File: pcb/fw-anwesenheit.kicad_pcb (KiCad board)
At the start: 6 copper layers, 50 x 50 mm, 48 parts, among them J1 Conn_01x02_Pin, J2 I2C, J3 LED, J4 MicroSD, U1 XIAO-ESP32-S3-SMD, U2 SN74AHCT1G125DBVT, U3 DS3231M

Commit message: changed via size
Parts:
- TP6: value SD_DECT -> DECT
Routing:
- net Net-(U1-GPIO16_D6_TX): track 41.7 -> 42.3 mm
- net GND: vias 107 -> 108

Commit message: changed some pcb descriptions and Resistor for LED
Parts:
- C2, C3: value 100 nF -> 100nF
- R1: value 100R -> 150R
- TP6: value DECT -> SD_DECT

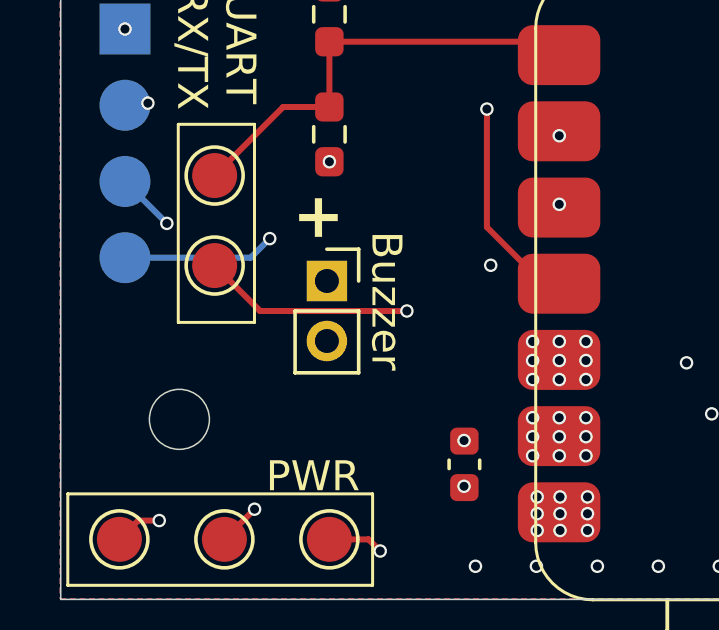
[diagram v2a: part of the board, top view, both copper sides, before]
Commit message: fixed buzzer footprint
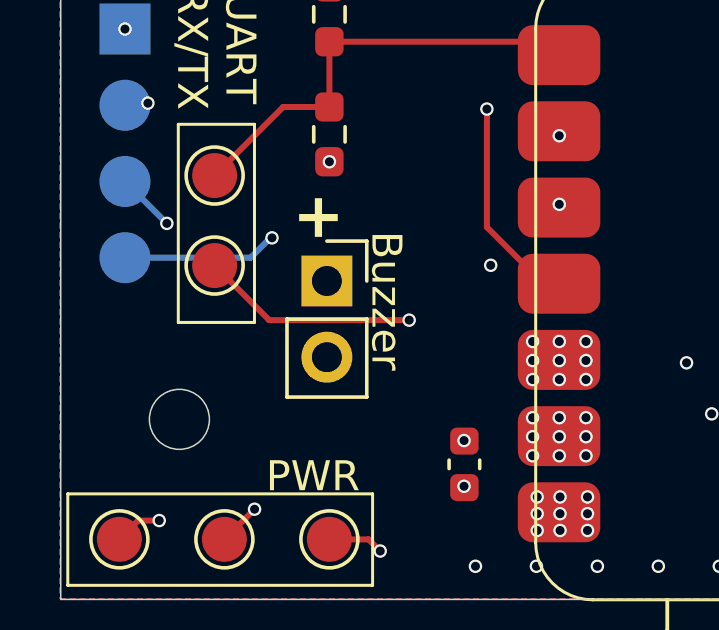
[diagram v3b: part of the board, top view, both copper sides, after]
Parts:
- BZ1: footprint Connector_PinSocket_2.00mm:PinSocket_1x02_P2.00mm_Vertical -> Connector_PinSocket_2.54mm:PinSocket_1x02_P2.54mm_Vertical
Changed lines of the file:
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@@
 		)
 	)
-	(footprint "Connector_PinSocket_2.00mm:PinSocket_1x02_P2.00mm_Vertical"
+	(footprint "Connector_PinSocket_2.54mm:PinSocket_1x02_P2.54mm_Vertical"
 		(layer "F.Cu")
 		(at 89.916 118.888)
-		(descr "Through hole straight socket strip, 1x02, 2.00mm pitch, single row (from Kicad 4.0.7), script generated")
-		(tags "Through hole socket strip THT 1x02 2.00mm single row")
+		(descr "Through hole straight socket strip, 1x02, 2.54mm pitch, single row (from Kicad 4.0.7), script generated")
+		(tags "Through hole socket strip THT 1x02 2.54mm single row")
 		(property "Reference" "BZ1"
-			(at 0 -2.5 0)
+			(at 0 -2.77 0)
 			(layer "F.SilkS")
 			(hide yes)
@@
 		)
 		(property "Value" "Buzzer"
-			(at 0 4.5 0)
+			(at 0 5.31 0)
 			(layer "F.Fab")
 			(hide yes)
@@
 		(attr through_hole)
 		(fp_line
-			(start -1.06 1)
-			(end -1.06 3.06)
+			(start -1.33 1.27)
+			(end -1.33 3.87)
 			(stroke
 				(width 0.12)
@@
 		)
 		(fp_line
-			(start -1.06 1)
-			(end 1.06 1)
+			(start -1.33 1.27)
+			(end 1.33 1.27)
 			(stroke
 				(width 0.12)
@@
 		)
 		(fp_line
-			(start -1.06 3.06)
-			(end 1.06 3.06)
+			(start -1.33 3.87)
+			(end 1.33 3.87)
 			(stroke
 				(width 0.12)
@@
 		)
 		(fp_line
-			(start 0 -1.06)
-			(end 1.06 -1.06)
+			(start 0 -1.33)
+			(end 1.33 -1.33)
 			(stroke
 				(width 0.12)
@@
 		)
 		(fp_line
-			(start 1.06 -1.06)
-			(end 1.06 0)
+			(start 1.33 -1.33)
+			(end 1.33 0)
 			(stroke
 				(width 0.12)
@@
 		)
 		(fp_line
-			(start 1.06 1)
-			(end 1.06 3.06)
+			(start 1.33 1.27)
+			(end 1.33 3.87)
 			(stroke
 				(width 0.12)
@@
 		)
 		(fp_line
-			(start -1.5 -1.5)
-			(end 1.5 -1.5)
+			(start -1.8 -1.8)
+			(end 1.75 -1.8)
 			(stroke
 				(width 0.05)
@@
 		)
 		(fp_line
-			(start -1.5 3.5)
-			(end -1.5 -1.5)
+			(start -1.8 4.3)
+			(end -1.8 -1.8)
 			(stroke
 				(width 0.05)
@@
 		)
 		(fp_line
-			(start 1.5 -1.5)
-			(end 1.5 3.5)
+			(start 1.75 -1.8)
+			(end 1.75 4.3)
 			(stroke
 				(width 0.05)
@@
 		)
 		(fp_line
-			(start 1.5 3.5)
-			(end -1.5 3.5)
+			(start 1.75 4.3)
+			(end -1.8 4.3)
 			(stroke
 				(width 0.05)
@@
 		)
 		(fp_line
-			(start -1 -1)
-			(end 0.5 -1)
+			(start -1.27 -1.27)
+			(end 0.635 -1.27)
 			(stroke
 				(width 0.1)
@@
 		)
 		(fp_line
-			(start -1 3)
-			(end -1 -1)
+			(start -1.27 3.81)
+			(end -1.27 -1.27)
 			(stroke
 				(width 0.1)
@@
 		)
 		(fp_line
-			(start 0.5 -1)
-			(end 1 -0.5)
+			(start 0.635 -1.27)
+			(end 1.27 -0.635)
 			(stroke
 				(width 0.1)
@@
 		)
 		(fp_line
-			(start 1 -0.5)
-			(end 1 3)
+			(start 1.27 -0.635)
+			(end 1.27 3.81)
 			(stroke
 				(width 0.1)
@@
 		)
 		(fp_line
-			(start 1 3)
-			(end -1 3)
+			(start 1.27 3.81)
+			(end -1.27 3.81)
 			(stroke
 				(width 0.1)
@@
 		)
 		(fp_text user "${REFERENCE}"
-			(at 0 1 90)
+			(at 0 1.27 90)
 			(layer "F.Fab")
 			(effects
@@
 		(pad "1" thru_hole rect
 			(at 0 0)
-			(size 1.35 1.35)
-			(drill 0.8)
+			(size 1.7 1.7)
+			(drill 1)
 			(layers "*.Cu" "*.Mask")
-			(remove_unused_layers yes)
-			(keep_end_layers yes)
-			(zone_layer_connections)
+			(remove_unused_layers no)
 			(net 18 "/Buzzer")
 			(pinfunction "+")
@@
 		)
 		(pad "2" thru_hole circle
-			(at 0 2)
-			(size 1.35 1.35)
-			(drill 0.8)
+			(at 0 2.54)
+			(size 1.7 1.7)
+			(drill 1)
 			(layers "*.Cu" "*.Mask")
-			(remove_unused_layers yes)
-			(keep_end_layers yes)
-			(zone_layer_connections "In1.Cu" "In2.Cu" "In3.Cu" "In4.Cu")
+			(remove_unused_layers no)
 			(net 1 "GND")
 			(pinfunction "-")
@@
 		)
 		(embedded_fonts no)
-		(model "${KICAD9_3DMODEL_DIR}/Connector_PinSocket_2.00mm.3dshapes/PinSocket_1x02_P2.00mm_Vertical.step"
+		(model "${KICAD9_3DMODEL_DIR}/Connector_PinSocket_2.54mm.3dshapes/PinSocket_1x02_P2.54mm_Vertical.step"
 			(offset
 				(xyz 0 0 0)
@@
 	)
 	(segment
-		(start 116.459 118.11)
-		(end 116.459 113.9959)
+		(start 87.9948 120.1928)
+		(end 86.302 118.5)
 		(width 0.2)
 		(layer "F.Cu")
@@
 	)
 	(segment
-		(start 116.459 113.9959)
-		(end 113.8216 111.3585)
+		(start 116.459 118.11)
+		(end 116.459 113.9959)
 		(width 0.2)
 		(layer "F.Cu")
@@
 	)
 	(segment
-		(start 116.078 118.491)
-		(end 116.459 118.11)
+		(start 92.6592 120.1928)
+		(end 87.9948 120.1928)
 		(width 0.2)
 		(layer "F.Cu")
@@
 	)
 	(segment
-		(start 87.69 119.888)
-		(end 92.583 119.888)
+		(start 116.459 113.9959)
+		(end 113.8216 111.3585)
 		(width 0.2)
 		(layer "F.Cu")
@@
 	)
 	(segment
-		(start 86.302 118.5)
-		(end 87.69 119.888)
+		(start 116.078 118.491)
+		(end 116.459 118.11)
 		(width 0.2)
 		(layer "F.Cu")
@@
 	)
 	(via
-		(at 92.583 119.888)
+		(at 92.6592 120.1928)
 		(size 0.45)
 		(drill 0.3)
@@
 	)
 	(segment
-		(start 103.4796 122.0216)
-		(end 101.346 119.888)
+		(start 114.5794 122.0216)
+		(end 116.078 120.523)
 		(width 0.2)
 		(layer "In3.Cu")
@@
 	)
 	(segment
-		(start 114.5794 122.0216)
-		(end 103.4796 122.0216)
+		(start 103.4796 122.0216)
+		(end 114.5794 122.0216)
 		(width 0.2)
 		(layer "In3.Cu")
@@
 	)
 	(segment
-		(start 116.078 120.523)
-		(end 114.5794 122.0216)
+		(start 92.6592 120.1928)
+		(end 101.6508 120.1928)
 		(width 0.2)
 		(layer "In3.Cu")
@@
 	)
 	(segment
-		(start 116.078 118.491)
-		(end 116.078 120.523)
+		(start 101.6508 120.1928)
+		(end 103.4796 122.0216)
 		(width 0.2)
 		(layer "In3.Cu")
@@
 	)
 	(segment
-		(start 101.346 119.888)
-		(end 92.583 119.888)
+		(start 116.078 120.523)
+		(end 116.078 118.491)
 		(width 0.2)
 		(layer "In3.Cu")
@@
 	)
 	(via
-		(at 88.011 117.475)
+		(at 88.0872 117.4496)
 		(size 0.45)
 		(drill 0.3)
@@
 	)
 	(segment
-		(start 83.185 118.11)
-		(end 87.376 118.11)
+		(start 87.376 118.11)
+		(end 83.185 118.11)
 		(width 0.2)
 		(layer "B.Cu")
@@
 	)
 	(segment
-		(start 87.376 118.11)
-		(end 88.011 117.475)
+		(start 88.0872 117.4496)
+		(end 88.0364 117.4496)
 		(width 0.2)
 		(layer "B.Cu")
@@
 	)
 	(segment
-		(start 109.474 97.282)
-		(end 109.22 97.282)
+		(start 88.0364 117.4496)
+		(end 87.376 118.11)
+		(width 0.2)
+		(layer "B.Cu")
+		(net 23)
+	)
+	(segment
+		(start 88.2142 117.475)
+		(end 115.57 117.475)
 		(width 0.2)
 		(layer "In3.Cu")
@@
 	)
 	(segment
-		(start 115.57 117.475)
-		(end 88.011 117.475)
+		(start 88.1888 117.4496)
+		(end 88.2142 117.475)
+		(width 0.2)
+		(layer "In3.Cu")
+		(net 23)
+	)
+	(segment
+		(start 109.474 97.282)
+		(end 109.22 97.282)
 		(width 0.2)
 		(layer "In3.Cu")
@@
 	)
 	(segment
-		(start 109.7915 97.5995)
-		(end 109.474 97.282)
+		(start 115.57 117.475)
+		(end 115.824 117.221)
 		(width 0.2)
 		(layer "In3.Cu")
@@
 	(segment
 		(start 115.824 117.221)
-		(end 115.57 117.475)
+		(end 115.824 117.094)
 		(width 0.2)
 		(layer "In3.Cu")
@@
 	)
 	(segment
-		(start 115.824 117.094)
-		(end 115.824 117.221)
+		(start 88.0872 117.4496)
+		(end 88.1888 117.4496)
+		(width 0.2)
+		(layer "In3.Cu")
+		(net 23)
+	)
+	(segment
+		(start 109.7915 97.5995)
+		(end 109.474 97.282)
 		(width 0.2)
 		(layer "In3.Cu")

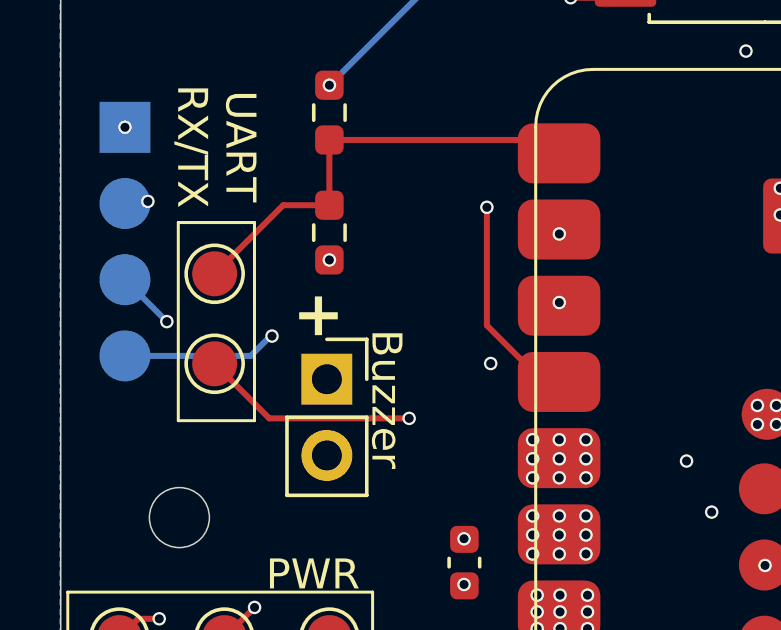
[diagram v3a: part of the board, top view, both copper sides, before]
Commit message: added some descriptions on pcb layout
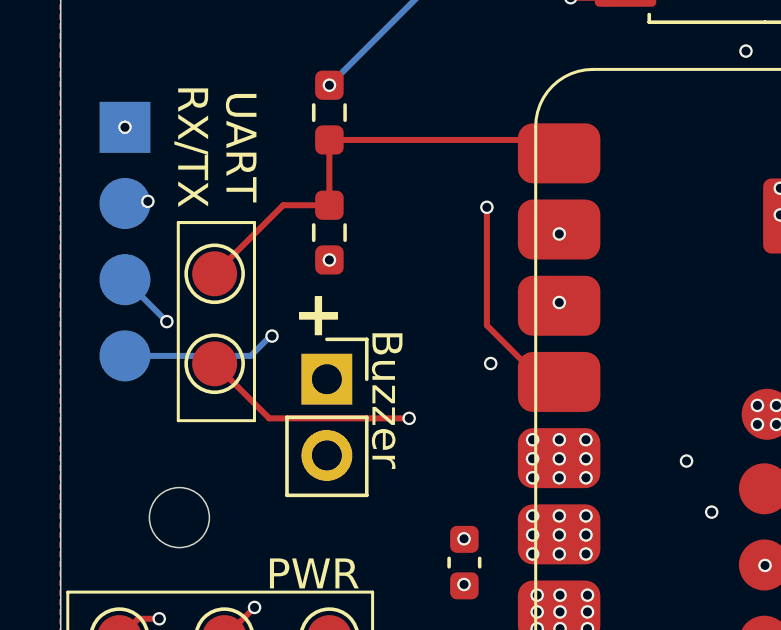
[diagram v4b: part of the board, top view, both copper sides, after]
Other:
- board text added: "DIN 5V GND"
- board text added: "LED"
